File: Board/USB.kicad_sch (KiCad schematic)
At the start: 30 parts, among them IC8 MAX3421E, Q2 32kHz, Q3 12MHz, X1 FPS009-300

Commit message: Ultipet 1.0A final
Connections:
- net 3.3V: no longer U$12.3V3 (V33)
- net SPI_CLK renamed SPI_CLK/CCLK

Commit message: ultipet 1.1a board
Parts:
- removed C150: 0.1u, cbm_ultipet_v1:C050-025X075, symbol cbm_ultipet_v1-eagle-import:C-EU050-025X075
- removed R17, R26: 10k, cbm_ultipet_v1:0204_7, symbol cbm_ultipet_v1-eagle-import:R-EU_0204/7
- removed R32: 33, cbm_ultipet_v1:0204_7, symbol cbm_ultipet_v1-eagle-import:R-EU_0204/7
- removed X1: FPS009-300, cbm_ultipet_v1:FPS009-3000, symbol cbm_ultipet_v1-eagle-import:FPS009-300
- added P10: ~, cbm_ultipet_v1:Pmod-SDCard, symbol SDCard:Pmod-SDCard
- added P4: ~, Connector_IDC:IDC-Header_2x05_P2.54mm_Vertical, symbol SPI:SPI-10-3V3
- IC8: footprint cbm_ultipet_v1:TQFP32-5MM -> Package_QFP:PQFP-32_5x5mm_P0.5mm
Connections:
- net DETECT: now also P10.9 (CD)
- net GND: now also P10.11 (GND), P10.5 (GND), P4.2 (GND)
- net OPENHIGH: now also IC8.27 (GPIN1)
- net SPI_CLK/CCLK: now also P10.4 (SCK), P4.9 (CLK)
- net SPI_IN3: now also P10.3 (MISO,D0)
- net SPI_MOSI: now also P10.2 (MOSI,CMD), P4.8 (MOSI)
- net SPI_NSEL3: now also P10.1 (/CS,D3)
- net 3.3V renamed V33
- net V33: now also P10.12 (V33), P10.6 (V33), P4.1 (VCC)
- new net SPI_MISO/DIN: P4.7 (MISO)
- new net SPI_NSEL0: P4.10 (/SEL)
- new net /IRQ: P4.6 (/IRQ)
- new net /RES: P4.5 (/RES)
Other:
- note added: "1.1A: - Add second (option for) SD-Card adapter - replace non-commercial use TQFP32 footprint with default kicad one"
- note added: "CBM-ULTIPET-V1.1A"
- note added: "CSA-ULTIPET-V1.1A-20240614"
- note removed: "CBM-ULTIPET-V1.0A"
- note removed: "CSA-ULTIPET-V1.0A-20240104"
- note removed: "Non-commercial use only"
- note removed: "Note: MAX3421 TQFP-5MM"
- note removed: "package layout by SparkFun"

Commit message: diverse fixes
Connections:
- net V33: no longer P10.12 (V33), P10.6 (V33), U$9.2_5 (V33)
- new net V33IO: P10.12 (V33), P10.6 (V33), U$9.2_5 (V33)
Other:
- note added: "1.1A: - Add second (option for) SD-Card adapter - replace non-commercial use TQFP32 footprint with default kicad one 1.2A: - use V33IO for Net and SD-Card"
- note added: "CBM-ULTIPET-V1.2A"
- note removed: "1.1A: - Add second (option for) SD-Card adapter - replace non-commercial use TQFP32 footprint with default kicad one"
- note removed: "CBM-ULTIPET-V1.1A"
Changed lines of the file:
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@@
 	(paper "User" 357.683 261.772)
 	(junction
-		(at 149.86 50.8)
-		(diameter 0)
-		(color 0 0 0 0)
-	)
-	(junction
 		(at 261.62 45.72)
 		(diameter 0)
@@
 	)
 	(junction
+		(at 148.59 50.8)
+		(diameter 0)
+		(color 0 0 0 0)
+	)
+	(junction
 		(at 86.36 109.22)
 		(diameter 0)
@@
 	(wire
 		(pts
-			(xy 149.86 50.8) (xy 149.86 49.53)
-		)
-		(stroke
-			(width 0)
-			(type default)
-		)
-	)
-	(wire
-		(pts
 			(xy 73.66 43.18) (xy 73.66 99.06)
 		)
@@
 	(wire
 		(pts
-			(xy 299.72 185.42) (xy 307.34 185.42)
-		)
-		(stroke
-			(width 0.1524)
-			(type solid)
-		)
-	)
-	(wire
-		(pts
 			(xy 129.54 205.74) (xy 134.62 205.74)
 		)
@@
 	(wire
 		(pts
-			(xy 144.78 53.34) (xy 149.86 53.34)
-		)
-		(stroke
-			(width 0)
-			(type default)
-		)
-	)
-	(wire
-		(pts
 			(xy 276.86 45.72) (xy 276.86 50.8)
 		)
@@
 	(wire
 		(pts
-			(xy 299.72 180.34) (xy 299.72 185.42)
-		)
-		(stroke
-			(width 0.1524)
-			(type solid)
-		)
-	)
-	(wire
-		(pts
 			(xy 269.24 60.96) (xy 269.24 66.04)
 		)
@@
 	(wire
 		(pts
-			(xy 144.78 50.8) (xy 149.86 50.8)
-		)
-		(stroke
-			(width 0)
-			(type default)
-		)
-	)
-	(wire
-		(pts
 			(xy 231.14 154.94) (xy 220.98 154.94)
 		)
@@
 	(wire
 		(pts
-			(xy 294.64 180.34) (xy 299.72 180.34)
-		)
-		(stroke
-			(width 0.1524)
-			(type solid)
-		)
-	)
-	(wire
-		(pts
 			(xy 109.22 114.3) (xy 106.68 114.3)
 		)
@@
 	(wire
 		(pts
+			(xy 298.45 184.15) (xy 302.26 184.15)
+		)
+		(stroke
+			(width 0)
+			(type default)
+		)
+	)
+	(wire
+		(pts
 			(xy 251.46 73.66) (xy 251.46 76.2)
 		)
@@
 	(wire
 		(pts
+			(xy 148.59 53.34) (xy 148.59 50.8)
+		)
+		(stroke
+			(width 0)
+			(type default)
+		)
+	)
+	(wire
+		(pts
 			(xy 248.92 68.58) (xy 256.54 68.58)
 		)
@@
 	(wire
 		(pts
+			(xy 298.45 184.15) (xy 298.45 180.34)
+		)
+		(stroke
+			(width 0)
+			(type default)
+		)
+	)
+	(wire
+		(pts
 			(xy 269.24 66.04) (xy 281.94 66.04)
 		)
@@
 	(wire
 		(pts
+			(xy 298.45 180.34) (xy 294.64 180.34)
+		)
+		(stroke
+			(width 0)
+			(type default)
+		)
+	)
+	(wire
+		(pts
 			(xy 91.44 152.4) (xy 55.88 152.4)
 		)
@@
 	(wire
 		(pts
+			(xy 144.78 53.34) (xy 148.59 53.34)
+		)
+		(stroke
+			(width 0)
+			(type default)
+		)
+	)
+	(wire
+		(pts
 			(xy 219.71 95.25) (xy 223.52 95.25)
 		)
@@
 	(wire
 		(pts
+			(xy 144.78 50.8) (xy 148.59 50.8)
+		)
+		(stroke
+			(width 0)
+			(type default)
+		)
+	)
+	(wire
+		(pts
 			(xy 121.92 121.92) (xy 116.84 121.92)
 		)
@@
 	(wire
 		(pts
-			(xy 124.46 43.18) (xy 73.66 43.18)
+			(xy 148.59 50.8) (xy 151.13 50.8)
 		)
 		(stroke
@@
 	(wire
 		(pts
-			(xy 149.86 53.34) (xy 149.86 50.8)
+			(xy 124.46 43.18) (xy 73.66 43.18)
 		)
 		(stroke
@@
 		)
 	)
-	(text "CBM-ULTIPET-V1.1A"
+	(text "CBM-ULTIPET-V1.2A"
 		(exclude_from_sim no)
 		(at 231.14 210.82 0)
@@
 		)
 	)
-	(text "1.1A:\n- Add second (option for) SD-Card adapter\n- replace non-commercial use TQFP32 footprint with default kicad one\n"
+	(text "1.1A:\n- Add second (option for) SD-Card adapter\n- replace non-commercial use TQFP32 footprint with default kicad one\n1.2A:\n- use V33IO for Net and SD-Card"
 		(exclude_from_sim no)
-		(at 109.728 233.426 0)
+		(at 109.728 231.648 0)
 		(effects
 			(font
@@
 		)
 	)
-	(global_label "V33"
-		(shape bidirectional)
-		(at 302.26 185.42 0)
-		(fields_autoplaced yes)
-		(effects
-			(font
-				(size 1.2446 1.2446)
-			)
-			(justify left)
-		)
-		(property "Intersheetrefs" "${INTERSHEET_REFS}"
-			(at 309.7116 185.42 0)
-			(effects
-				(font
-					(size 1.27 1.27)
-				)
-				(justify left)
-				(hide yes)
-			)
-		)
-	)
 	(global_label "SPI_CLK{slash}CCLK"
 		(shape input)
@@
 		)
 	)
+	(global_label "V33IO"
+		(shape input)
+		(at 302.26 184.15 0)
+		(fields_autoplaced yes)
+		(effects
+			(font
+				(size 1.27 1.27)
+			)
+			(justify left)
+		)
+		(property "Intersheetrefs" "${INTERSHEET_REFS}"
+			(at 310.6881 184.15 0)
+			(effects
+				(font
+					(size 1.27 1.27)
+				)
+				(justify left)
+				(hide yes)
+			)
+		)
+	)
 	(global_label "VBUF"
 		(shape bidirectional)
@@
 		)
 	)
+	(global_label "V33IO"
+		(shape input)
+		(at 151.13 50.8 0)
+		(fields_autoplaced yes)
+		(effects
+			(font
+				(size 1.27 1.27)
+			)
+			(justify left)
+		)
+		(property "Intersheetrefs" "${INTERSHEET_REFS}"
+			(at 159.5581 50.8 0)
+			(effects
+				(font
+					(size 1.27 1.27)
+				)
+				(justify left)
+				(hide yes)
+			)
+		)
+	)
 	(global_label "SPI_MOSI"
 		(shape bidirectional)
@@
 					(unit 1)
 				)
-			)
-		)
-	)
-	(symbol
-		(lib_id "cbm_ultipet_v1-eagle-import:3.3V")
-		(at 149.86 49.53 0)
-		(unit 1)
-		(exclude_from_sim no)
-		(in_bom yes)
-		(on_board yes)
-		(dnp no)
-		(property "Reference" "#P+07"
-			(at 149.86 49.53 0)
-			(effects
-				(font
-					(size 1.27 1.27)
-				)
-				(hide yes)
-			)
-		)
-		(property "Value" "V33"
-			(at 148.844 45.974 0)
-			(effects
-				(font
-					(size 1.778 1.5113)
-				)
-				(justify left bottom)
-			)
-		)
-		(property "Footprint" ""
-			(at 149.86 49.53 0)
-			(effects
-				(font
-					(size 1.27 1.27)
-				)
-				(hide yes)
-			)
-		)
-		(property "Datasheet" ""
-			(at 149.86 49.53 0)
-			(effects
-				(font
-					(size 1.27 1.27)
-				)
-				(hide yes)
-			)
-		)
-		(property "Description" ""
-			(at 149.86 49.53 0)
-			(effects
-				(font
-					(size 1.27 1.27)
-				)
-				(hide yes)
-			)
-		)
-		(pin "1"
-		)
-		(instances
-			(project "cbm_ultipet_v1"
-				(path "/4dd2dd78-173f-4b46-8cce-4ed940435c94/d2c8cba7-54fd-4ca0-bac7-9d690d7d8e89"
-					(reference "#P+07")
-					(unit 1)
-				)

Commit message: more layout work
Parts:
- renumbered C21 to C22, C9 to C24
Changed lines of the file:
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@@
 		(on_board yes)
 		(dnp no)
-		(property "Reference" "C21"
+		(property "Reference" "C22"
 			(at 138.684 207.899 0)
 			(effects
@@
 			(project "cbm_ultipet_v1"
 				(path "/4dd2dd78-173f-4b46-8cce-4ed940435c94/d2c8cba7-54fd-4ca0-bac7-9d690d7d8e89"
-					(reference "C21")
+					(reference "C22")
 					(unit 1)
 				)
@@
 		(on_board yes)
 		(dnp no)
-		(property "Reference" "C9"
+		(property "Reference" "C24"
 			(at 148.844 207.899 0)
 			(effects
@@
 			(project "cbm_ultipet_v1"
 				(path "/4dd2dd78-173f-4b46-8cce-4ed940435c94/d2c8cba7-54fd-4ca0-bac7-9d690d7d8e89"
-					(reference "C9")
-					(unit 1)
-				)
+					(reference "C24")
+					(unit 1)
+				)

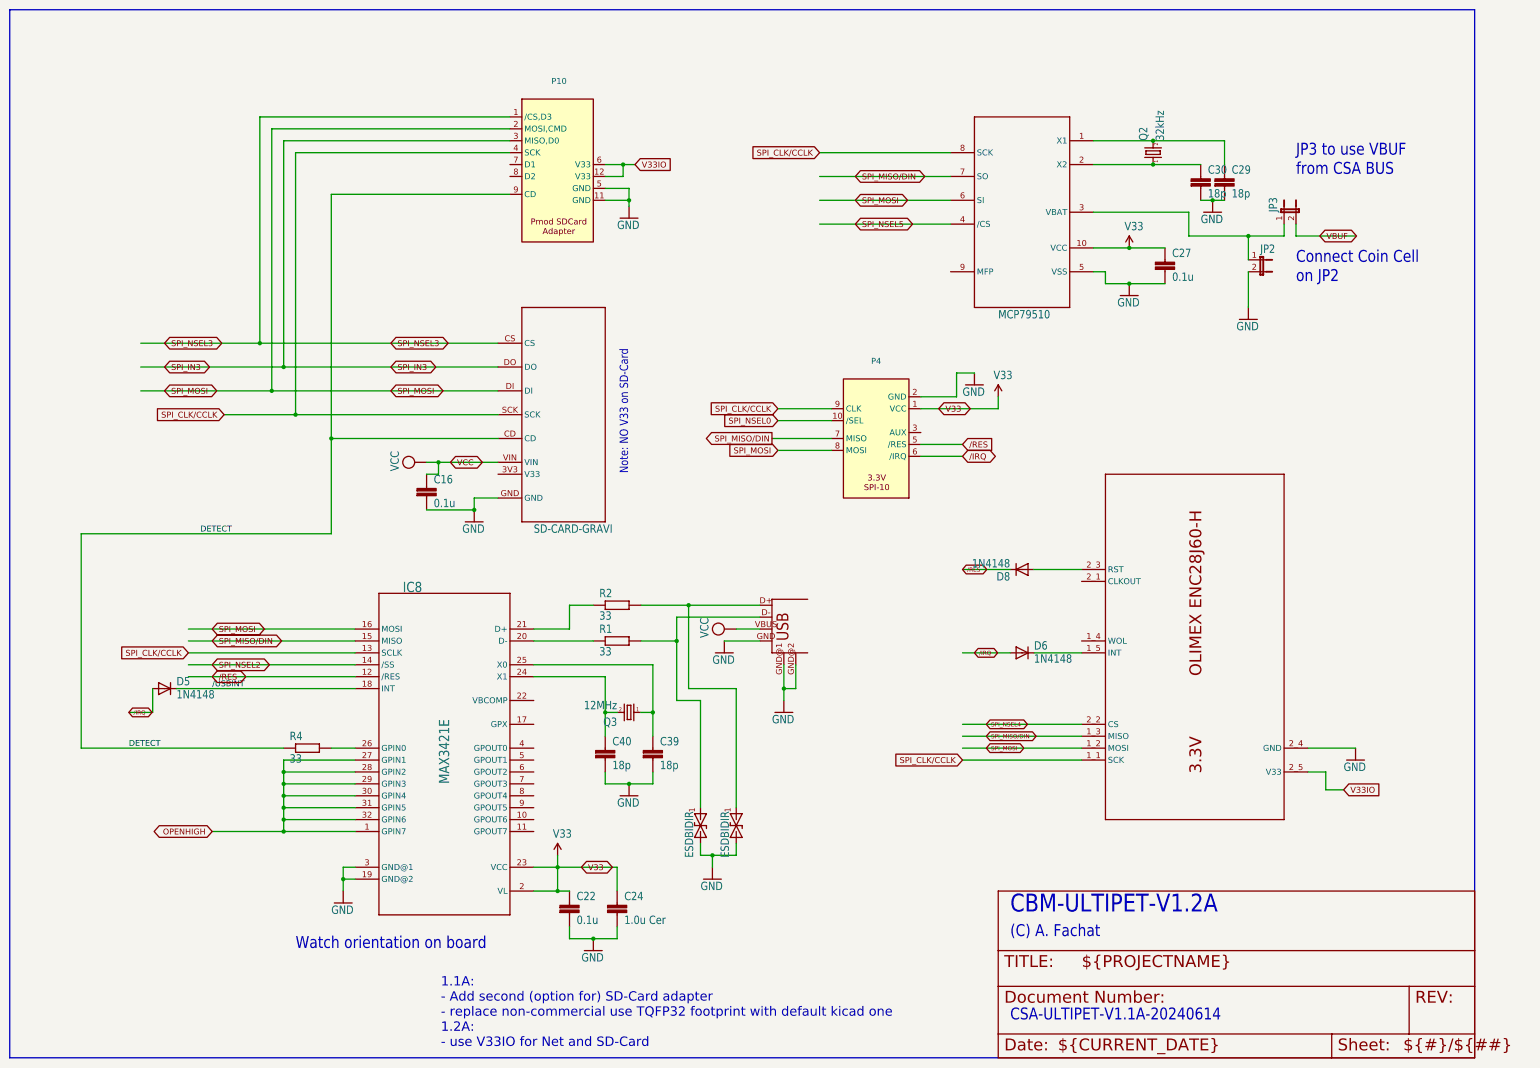
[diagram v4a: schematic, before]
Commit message: add bypass caps for SD Cards
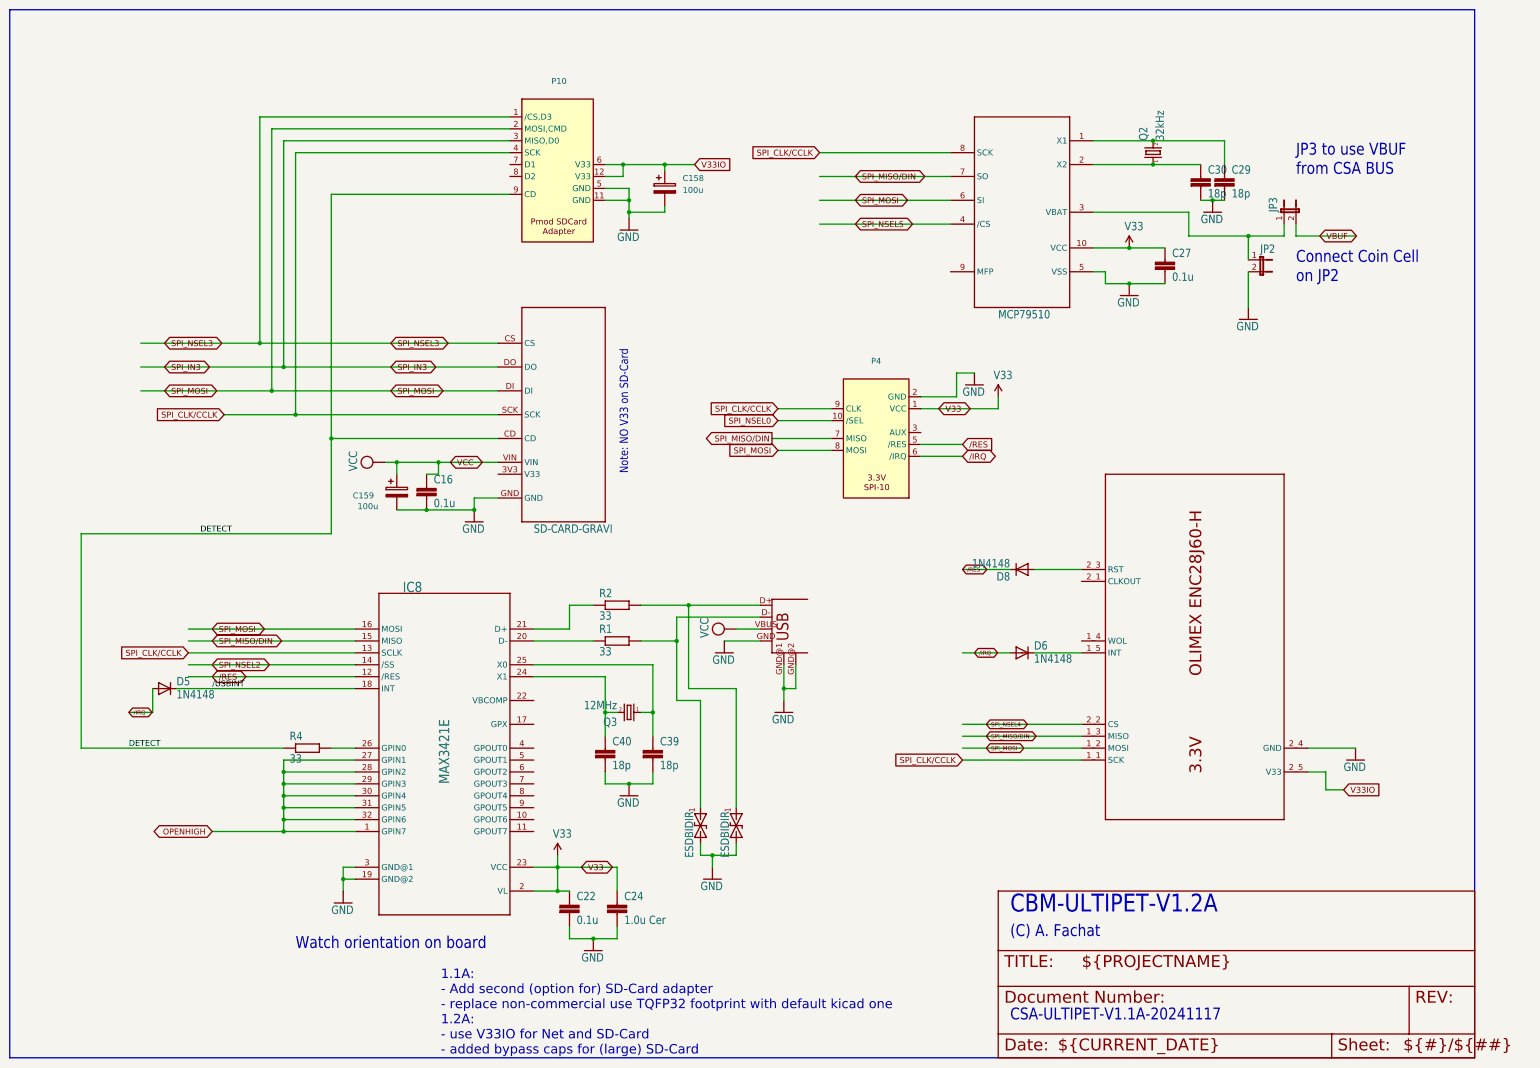
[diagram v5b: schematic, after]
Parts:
- added C158, C159: 100u, Capacitor_THT:CP_Radial_D5.0mm_P2.50mm, symbol Device:C_Polarized
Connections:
- net GND: now also C158.2, C159.2
- net V33IO: now also C158.1
- net VCC: now also C159.1
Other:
- note added: "1.1A: - Add second (option for) SD-Card adapter - replace non-commercial use TQFP32 footprint with default kicad one 1.2A: - use V33IO for Net and SD-Card - added bypass caps for (large) SD-Card"
- note added: "CSA-ULTIPET-V1.1A-20241117"
- note removed: "1.1A: - Add second (option for) SD-Card adapter - replace non-commercial use TQFP32 footprint with default kicad one 1.2A: - use V33IO for Net and SD-Card"
- note removed: "CSA-ULTIPET-V1.1A-20240614"

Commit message: replace some ultipet specific TQFP with easier to solder parts
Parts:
- IC8: footprint Package_QFP:PQFP-32_5x5mm_P0.5mm -> cbm_ultipet_v1:TQFP32-5MM
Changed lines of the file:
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@@
 			)
 		)
-		(property "Footprint" "Package_QFP:PQFP-32_5x5mm_P0.5mm"
+		(property "Footprint" "cbm_ultipet_v1:TQFP32-5MM"
 			(at 116.84 165.1 0)
 			(effects

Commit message: more work on 1.3
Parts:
- IC8: footprint cbm_ultipet_v1:TQFP32-5MM -> Package_QFP:LQFP-32_5x5mm_P0.5mm
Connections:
- net SPI_CLK/CCLK: no longer P4.9 (CLK)
- new net BUF_SPI_CLK: P4.9 (CLK)
